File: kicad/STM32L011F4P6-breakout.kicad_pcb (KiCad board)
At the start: 2 copper layers, 17 x 34 mm, 11 parts

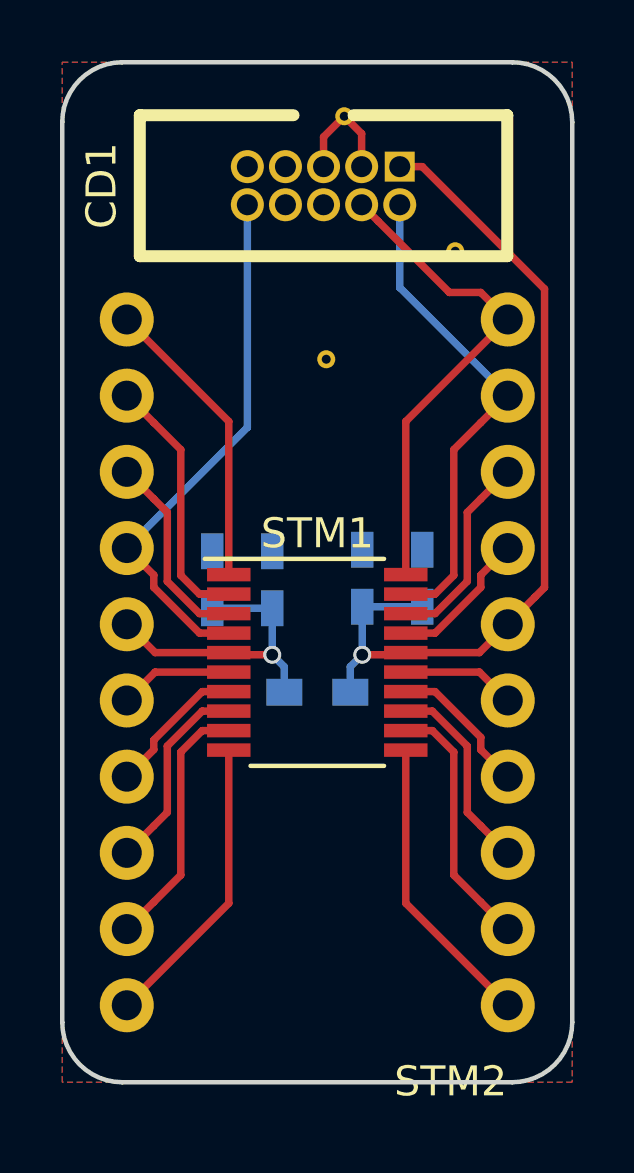
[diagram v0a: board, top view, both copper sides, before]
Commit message: moved STM down and rotated debug connector
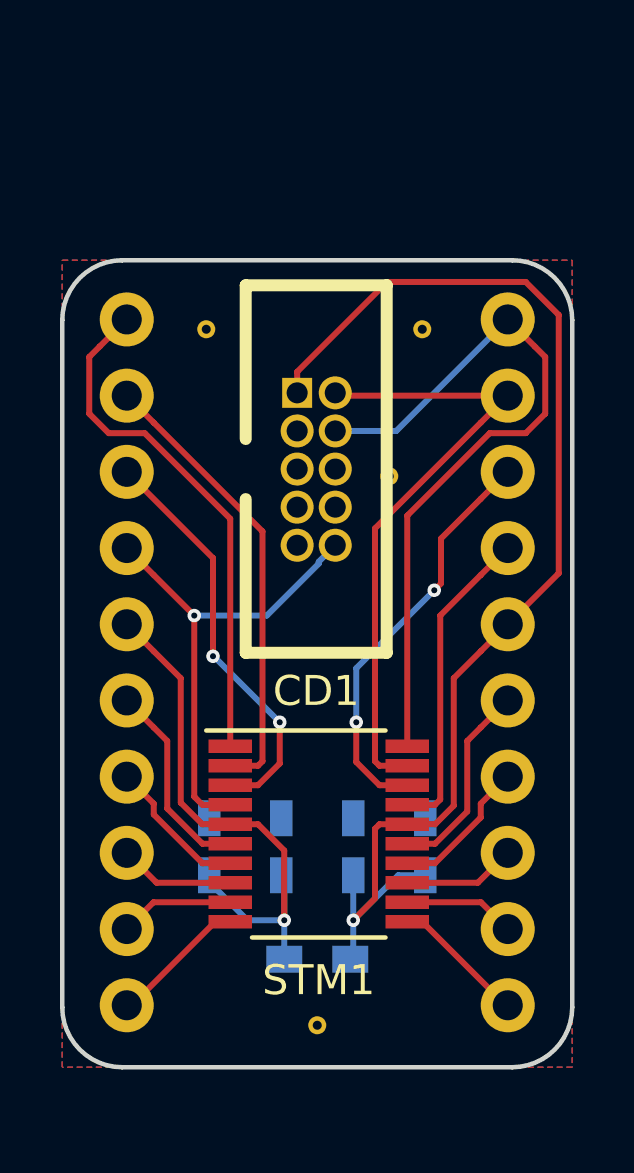
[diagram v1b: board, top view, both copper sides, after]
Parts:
- removed the REF** at (148.8, 94.9)
- added REF**: STITCHING_VIA, utils:STITCHING_VIA, F.Cu at (150.9, 98.8)
- added REF**: STITCHING_VIA, utils:STITCHING_VIA, F.Cu at (148.5, 117.1)
- moved CD1 9.45 mm to (148.5, 98.6), turned to 0 degrees
- moved C2 9.19 mm to (147.3, 111.2)
- moved C1 9.14 mm to (144.9, 111.2)
- moved C3 8.96 mm to (149.7, 111.2)
- moved C4 8.95 mm to (152.1, 111.2)
- moved L1 8.90 mm to (148.5, 114.9)
- moved REF** 8.46 mm to (144.8, 93.9)
- moved STM1 5.72 mm to (148.6, 110.7)
- moved REF** 2.82 mm to (152.0, 93.9)
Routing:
- net Net-(C3-Pad1): track 28.5 -> 41.1 mm
- net Net-(C1-Pad1): track 10.2 -> 19.2 mm
- net /SWDCLK: track 16.4 -> 24.6 mm
- net /PB9: track 9.91 -> 17.4 mm
- net /PC15: track 6.70 -> 13.8 mm, vias 0 -> 2
- net /PA10: track 6.70 -> 13.8 mm, vias 0 -> 2
- net /PC14: track 8.59 -> 15.2 mm
- net /PA9: track 4.81 -> 10.5 mm
- net /PA5: track 9.91 -> 4.50 mm
- net /PA4: track 9.91 -> 4.60 mm
- net /PA6: track 8.54 -> 3.72 mm
- net /PA3: track 8.54 -> 3.82 mm
- net /SWDIO: track 16.4 -> 20.9 mm
- net /PA0: track 3.79 -> 6.75 mm
- net /PA7: track 6.65 -> 3.76 mm
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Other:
- board size 17 x 34 mm -> 17 x 26.9 mm
- net class Default: clearance 0.2 -> 0.1; trace_width 0.25 -> 0.2; via_dia 0.6 -> 0.45; via_drill 0.4 -> 0.2
- rule trace_clearance: 0.2 -> 0.1
- rule trace_min: 0.2 -> 0.1
- rule via_min_drill: 0.3 -> 0.2
- rule via_min_size: 0.4 -> 0.45

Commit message: aligned footprints and added pin labels
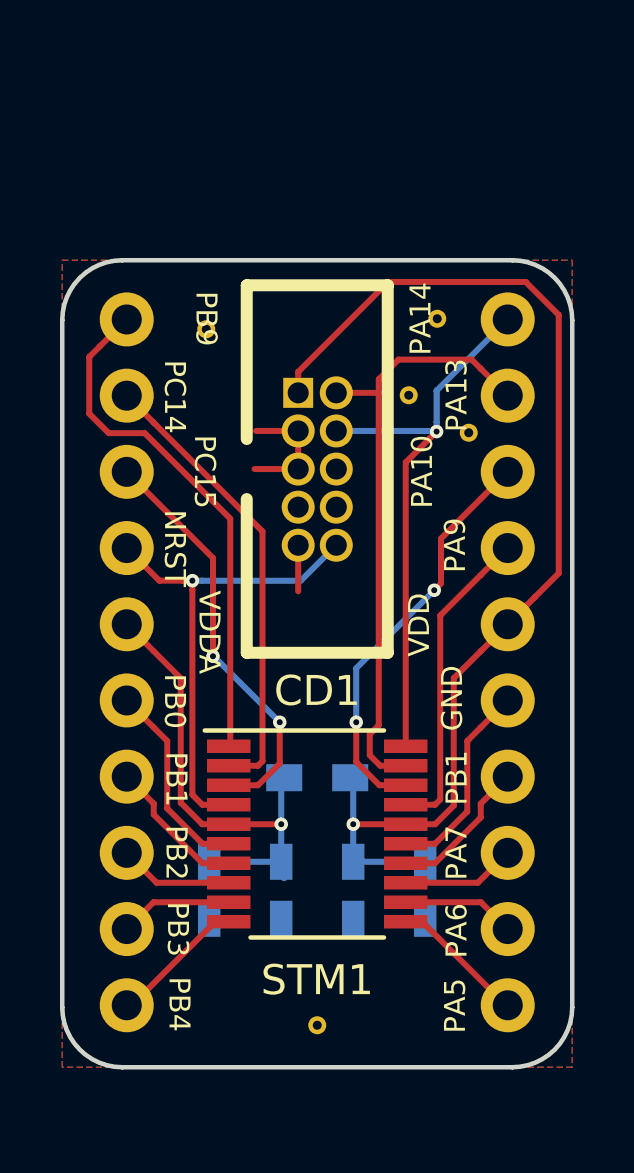
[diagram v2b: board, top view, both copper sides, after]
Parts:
- removed the REF** at (150.9, 98.8)
- added REF**: STITCHING_VIA, utils:STITCHING_VIA, F.Cu at (151.6, 96.1)
- added REF**: STITCHING_VIA, utils:STITCHING_VIA, F.Cu at (153.6, 97.3)
- moved L1 6.05 mm to (148.5, 108.8)
- moved C1 1.45 mm to (144.9, 112.6), turned to 270 degrees
- moved C2 1.45 mm to (147.3, 112.6), turned to 270 degrees
- moved C3 1.45 mm to (149.7, 112.6), turned to 270 degrees
- moved C4 1.45 mm to (152.1, 112.6), turned to 270 degrees
- moved REF** 0.61 mm to (152.5, 93.5)
- moved STM1 0.05 mm to (148.5, 110.7)
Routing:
- net GND: track 6.71 -> 12.4 mm
- net /SWDCLK: track 24.6 -> 19.0 mm, vias 0 -> 1
- net Net-(C3-Pad1): track 41.1 -> 37.7 mm
- net Net-(C1-Pad1): track 19.2 -> 16.0 mm
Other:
- board text added: "GND"
- board text added: "NRST"
- board text added: "PA10"
- board text added: "PA13"
- board text added: "PA14"
- board text added: "PA5"
- board text added: "PA6"
- board text added: "PA7"
- board text added: "PA9"
- board text added: "PB0"
- board text added: "PB1"
- board text added: "PB2"
- board text added: "PB3"
- board text added: "PB4"
- board text added: "PB9"
- board text added: "PC14"
- board text added: "PC15"
- board text added: "STM32L011F4P6 hochreiner.net"
- board text added: "VDD"
- board text added: "VDDA"
